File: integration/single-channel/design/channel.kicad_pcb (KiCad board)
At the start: 4 copper layers, 138 x 52 mm, 47 parts, among them J1 MCX edge jack 50R, J2 MCX edge jack 50R, J3 MCX edge jack 50R, J4 MCX edge jack 50R, J5 Screw terminal 3-pos 5.08mm, U1 CR-112, U2 CR-200-1us, U3 CR-210, U4 THS3491

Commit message: single-channel: Update PCB from Schematic (GUI) - library-prefixed footprint IDs + MPN fields
User's KiCad edits: 'Update PCB from Schematic' re-linked footprints and pushed the library
nickname onto each FPID (C_0805_2012Metric -> Capacitor_SMD:C_0805_2012Metric) plus the
MPN/Manufacturer/Distributor PN symbol fields onto the footprints. Metadata only - footprint/
track/via/zone counts unchanged (47/171/41/4), no geometry changed.

Co-Authored-By: Claude Opus 4.8 <noreply@anthropic.com>
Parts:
- C1, C12, C13, C2, C3, C4, C5, C6, C7, C8, C9: footprint C_0805_2012Metric -> Capacitor_SMD:C_0805_2012Metric
- C10, C11: footprint CP_Elec_6.3x7.7 -> Capacitor_SMD:CP_Elec_6.3x7.7
- D1, D2: footprint D_SMA -> Diode_SMD:D_SMA
- F1, F2: footprint Fuse_1206_3216Metric -> Fuse:Fuse_1206_3216Metric
- J1, J2, J3, J4: footprint MCX_CONMCX013_EdgeMount -> cremat:MCX_CONMCX013_EdgeMount
- J5: footprint TerminalBlock_Phoenix_MKDS-1,5-3_1x03_P5.00mm_Horizontal -> TerminalBlock_Phoenix:TerminalBlock_Phoenix_MKDS-1,5-3_1x03_P5.00mm_Horizontal
- R1, R10, R11, R12, R13, R14, R15, R16, R17, R18, R2, R3, R4, R5, R6, R7, R8, R9: footprint R_0805_2012Metric -> Resistor_SMD:R_0805_2012Metric
- RV1: footprint Potentiometer_Bourns_3296W_Vertical -> Potentiometer_THT:Potentiometer_Bourns_3296W_Vertical
- U1, U2, U3: footprint PinHeader_1x08_P2.54mm_Vertical -> Connector_PinHeader_2.54mm:PinHeader_1x08_P2.54mm_Vertical
- U4: footprint SOIC-8-1EP_3.9x4.9mm_P1.27mm_EP2.29x3mm -> Package_SO:SOIC-8-1EP_3.9x4.9mm_P1.27mm_EP2.29x3mm
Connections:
- C12 pad 1: /BVP -> unconnected-(C12-Pad1)
- C13 pad 1: /BVN -> unconnected-(C13-Pad1)
- C4 pad 1: /+VS_F -> unconnected-(C4-Pad1)
- C5 pad 1: /-VS_F -> unconnected-(C5-Pad1)
- C6 pad 1: /SHVP -> unconnected-(C6-Pad1)
- C7 pad 1: /SHVN -> unconnected-(C7-Pad1)
- C8 pad 1: /BLVP -> unconnected-(C8-Pad1)
- C9 pad 1: /BLVN -> unconnected-(C9-Pad1)
- R1 pad 2: /N_filt -> Net-(R1-Pad2)
- R10 pad 2: /BLVP -> unconnected-(R10-Pad2)
- R11 pad 2: /BLVN -> unconnected-(R11-Pad2)
- R13 pad 1: /BUF_OUT -> Net-(R13-Pad1)
- R16 pad 2: /BVP -> unconnected-(R16-Pad2)
- R17 pad 2: /BVN -> unconnected-(R17-Pad2)
- R18 pad 1: /SHAPER_OUT -> unconnected-(R18-Pad1)
- R18 pad 2: /BUF_OUT -> Net-(R13-Pad1)
- R2 pad 2: /N_filt -> Net-(R1-Pad2)
- R3 pad 1: /N_filt -> Net-(R1-Pad2)
- R4 pad 1: /N_filt -> Net-(R1-Pad2)
- R5 pad 1: /TEST_IN -> unconnected-(R5-Pad1)
- R6 pad 2: /+VS_F -> unconnected-(R6-Pad2)
- R7 pad 2: /-VS_F -> unconnected-(R7-Pad2)
- R8 pad 2: /SHVP -> unconnected-(R8-Pad2)
- R9 pad 2: /SHVN -> unconnected-(R9-Pad2)
- RV1 pad 1: /CSP_OUT -> unconnected-(RV1-Pad1)
- U4 pad 2: /BUF_FB -> unconnected-(U4---Pad2)

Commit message: single-channel: edge-mount MCX (user's Linx CONMCX013-T footprint) + connector orientation fixes
- Swap MCX to the user-downloaded cremat:MCX_CONMCX013-T (shield tabs G1/G2 -> pad 2 so
  GND connects via Conn_Coaxial pin 2; trimmed the connector-tiling edge-extension
  Edge.Cuts segments). Update gen_sch FP_MCX + gen_pcb .kicad_dru condition.
- MCX 3D model rotate (xyz 270 0 0): coax mating face now points OFF the board edge
  (raw STEP had it vertical/up). 3D-cosmetic patch to the routed board, no reroute.
- Fix the MCX edge-notch generator: place jacks by footprint origin (rot 90/270), outline
  cuts the notch read back from each placed MCX, demote footprint Edge.Cuts -> Dwgs.User,
  keep cremat: FPID prefix; write_dru() waives edge_clearance for the shield tabs.
- J5 screw terminal rot 0 -> 180 so the wire funnels face the top edge (was inward).
- Re-autorouted (FreeRouting / Java 25, dead-proxy headless recipe in docs/FREEROUTING.md):
  DRC 0 errors / 0 unconnected (4 benign lib_footprint_mismatch from the Edge.Cuts demotion).
- ERC 0; netlist membership identical to baseline (footprint field only, circuit unchanged).
- Add docs/HARDWARE_DEV_PLAYBOOK.md; SESSION_LOG records the ${KIPRJMOD} 3D-render gotcha.

Co-Authored-By: Claude Opus 4.8 <noreply@anthropic.com>
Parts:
- J1, J2, J3, J4: footprint cremat:MCX_CONMCX013_EdgeMount -> cremat:MCX_CONMCX013-T
- moved J5 10.0 mm to (29.0, 8.83), turned to 180 degrees
- moved J2 0.33 mm to (6.30, 29.0), turned to -90 degrees
- moved J3 0.33 mm to (6.30, 41.0), turned to -90 degrees
- moved J1 0.33 mm to (131.7, 41.0), turned to 90 degrees
- moved J4 0.33 mm to (131.7, 29.0), turned to 90 degrees
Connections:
- C12 pad 1: unconnected-(C12-Pad1) -> /BVP
- C13 pad 1: unconnected-(C13-Pad1) -> /BVN
- C4 pad 1: unconnected-(C4-Pad1) -> /+VS_F
- C5 pad 1: unconnected-(C5-Pad1) -> /-VS_F
- C6 pad 1: unconnected-(C6-Pad1) -> /SHVP
- C7 pad 1: unconnected-(C7-Pad1) -> /SHVN
- C8 pad 1: unconnected-(C8-Pad1) -> /BLVP
- C9 pad 1: unconnected-(C9-Pad1) -> /BLVN
- R1 pad 2: Net-(R1-Pad2) -> /N_filt
- R10 pad 2: unconnected-(R10-Pad2) -> /BLVP
- R11 pad 2: unconnected-(R11-Pad2) -> /BLVN
- R13 pad 1: Net-(R13-Pad1) -> /BUF_OUT
- R16 pad 2: unconnected-(R16-Pad2) -> /BVP
- R17 pad 2: unconnected-(R17-Pad2) -> /BVN
- R18 pad 1: unconnected-(R18-Pad1) -> /SHAPER_OUT
- R18 pad 2: Net-(R13-Pad1) -> /BUF_OUT
- R2 pad 2: Net-(R1-Pad2) -> /N_filt
- R3 pad 1: Net-(R1-Pad2) -> /N_filt
- R4 pad 1: Net-(R1-Pad2) -> /N_filt
- R5 pad 1: unconnected-(R5-Pad1) -> /TEST_IN
- R6 pad 2: unconnected-(R6-Pad2) -> /+VS_F
- R7 pad 2: unconnected-(R7-Pad2) -> /-VS_F
- R8 pad 2: unconnected-(R8-Pad2) -> /SHVP
- R9 pad 2: unconnected-(R9-Pad2) -> /SHVN
- RV1 pad 1: unconnected-(RV1-Pad1) -> /CSP_OUT
- U4 pad 2: unconnected-(U4---Pad2) -> /BUF_FB
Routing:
- net /+VDC_IN: track 19.7 -> 9.59 mm
- net /-VDC_IN: track 11.2 -> 21.3 mm
- net /OUT_50: track 26.0 -> 21.0 mm
- net /TEST_IN: track 24.8 -> 19.8 mm
- net /BVP: track 13.9 -> 18.3 mm, vias 2 -> 0
- net /BUF_OUT: track 31.2 -> 35.3 mm, vias 2 -> 0
- net /FE: track 38.3 -> 34.6 mm
- net /BIAS_IN: track 126.7 -> 123.7 mm
- net /SH_OUT: track 27.7 -> 29.5 mm, vias 1 -> 0
- net /BVN: track 19.3 -> 20.5 mm
- net /CSP_IN: track 20.7 -> 19.5 mm
- net /BUF_FB: track 16.6 -> 17.1 mm, vias 0 -> 2
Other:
- outline, holes or cut-outs redrawn

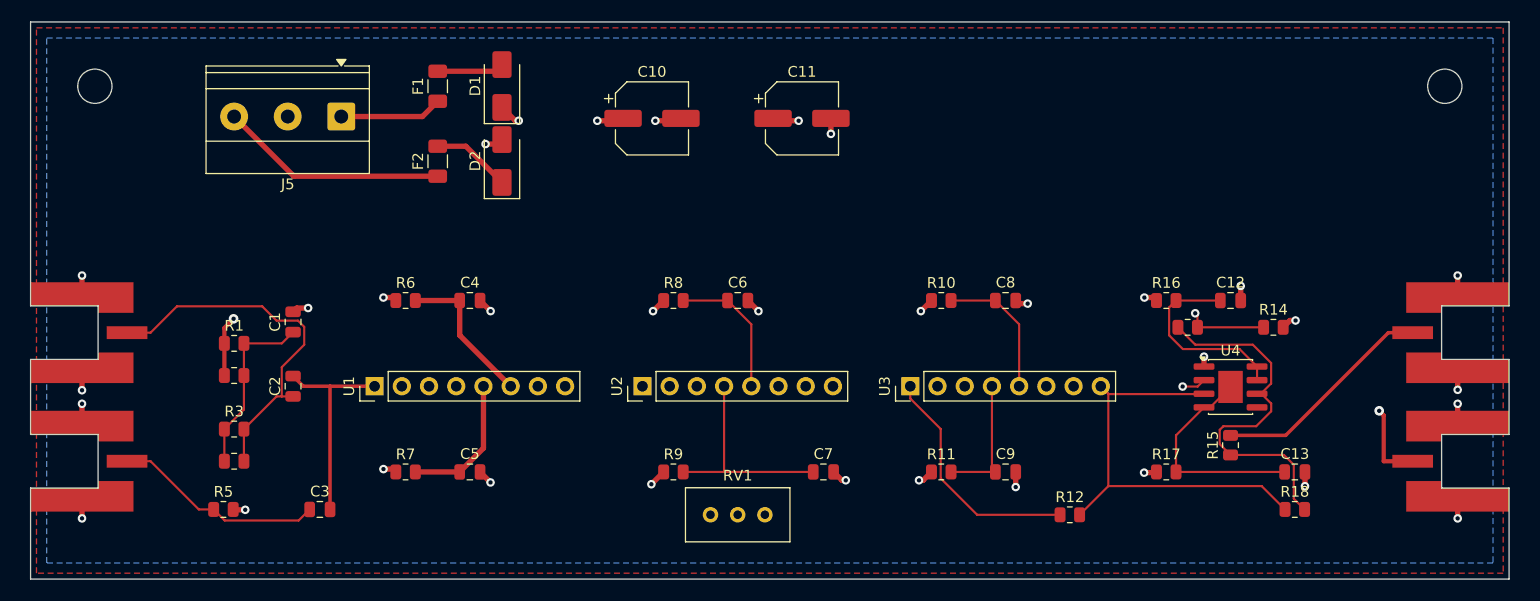
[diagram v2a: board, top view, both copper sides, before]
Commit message: 12ch order-ready v2: socketed Cremat modules, HV-DRC fix, 1U slot-through, JLC+DigiKey ordering package
Four workstreams, all gated (ERC 0 / netlist membership identical / DRC 0 errors,
0 unconnected, 0 parity with hv_bias verified live / renders checked):

SIP-8 sockets (never solder the modules):
- All 36 module sites -> stock PinSocket_1x08 footprint (pad+courtyard identical to the
  old header placeholder). Part: Samtec SS-108-TT-2 (DK 612-SS-108-TT-2-ND) - Cremat's
  own eval-board socket; accepts the modules' 0.51x0.25mm flat pins (live-verified).
  Alt: Harwin D01-9970842. NOT Mill-Max/Preci-Dip 801 (0.7-0.9mm pins).

hv_bias 0.6mm DRC rule was silently disabled - found and fixed at the source:
- Single-channel netclass patterns 'FE'/'N_filt' lacked the leading slash and matched
  nothing -> the 07-11 reroute packed the SiPM-bias front-end at 0.2mm. Patterns now
  '*/'-prefixed; single channel re-routed with the HV rule live in the DSN; 12ch re-tiled.
- A KiCad GUI save flattened twelve-channel.kicad_pro netclasses TWICE (DRC passed
  vacuously). Pipeline now self-heals: gen_pcb re-asserts build_pro() after SaveBoard;
  fill_zones refuses to fill blind (restores netclasses + loud warning).

Enclosure: 2U -> 1U, one board per case, slot-through panels:
- Hammond RM1U1908VBK (vented; ~13W under a 40mm lid). Factory-drawing-verified:
  internal 196.85 depth x 40.09 height; socketed module stack ~32mm -> fits.
- Board W 180 -> 213.2mm: passes through a ~340x7mm milled slot in each front/rear
  panel, protruding 5mm; MCX faces ~8.6mm proud, snap-on fully in the open. Slot
  machining spec in design/SESSION_LOG.md session 14.

Ordering (ORDERING.md = master buy sheet):
- JLCPCB fab + Economic SMT assembly (live-verified incl. wizard quote: ~$74/5 boards
  HASL, large-size fee $5; Economic tier OK, edge notches OK). Package in design/fab/jlc:
  gerber zip + JLC BOM (12 lines, LCSC C-numbers, 8 Basic / 4 Extended) + CPL (246
  FIT-SMD placements). Subs documented: 10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
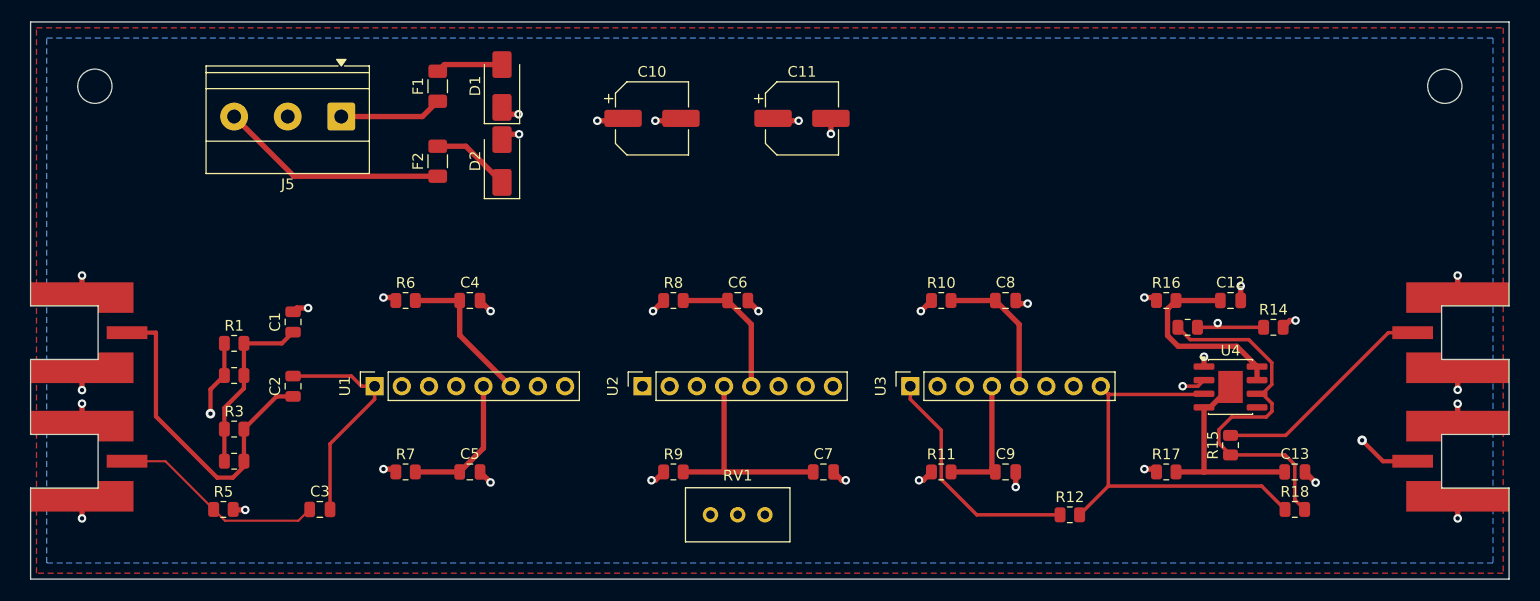
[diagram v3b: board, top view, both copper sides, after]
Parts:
- U1, U2, U3: footprint Connector_PinHeader_2.54mm:PinHeader_1x08_P2.54mm_Vertical -> Connector_PinSocket_2.54mm:PinSocket_1x08_P2.54mm_Vertical
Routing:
- net /FE: track 34.6 -> 30.9 mm
- net /BIAS_IN: track 123.7 -> 121.1 mm
- net /CSP_IN: track 19.5 -> 21.2 mm
- net /BUF_FB: track 17.1 -> 16.0 mm
- net /BVN: track 20.5 -> 19.4 mm
- net /CSP_OUT: track 28.8 -> 27.8 mm
- net /BUF_OUT: track 35.3 -> 35.8 mm
